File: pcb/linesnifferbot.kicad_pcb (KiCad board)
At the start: 2 copper layers, 100 x 99.5 mm, 78 parts, among them J10 CONN_01X09, J3 RxSel, J4 TxSel, J5 IntSelA, J6 IntSelB, J7 CONN_01X06, J8 Btn2EN, J9 LED2EN, Q1 Q_NMOS_GSD, SW1 SPDT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

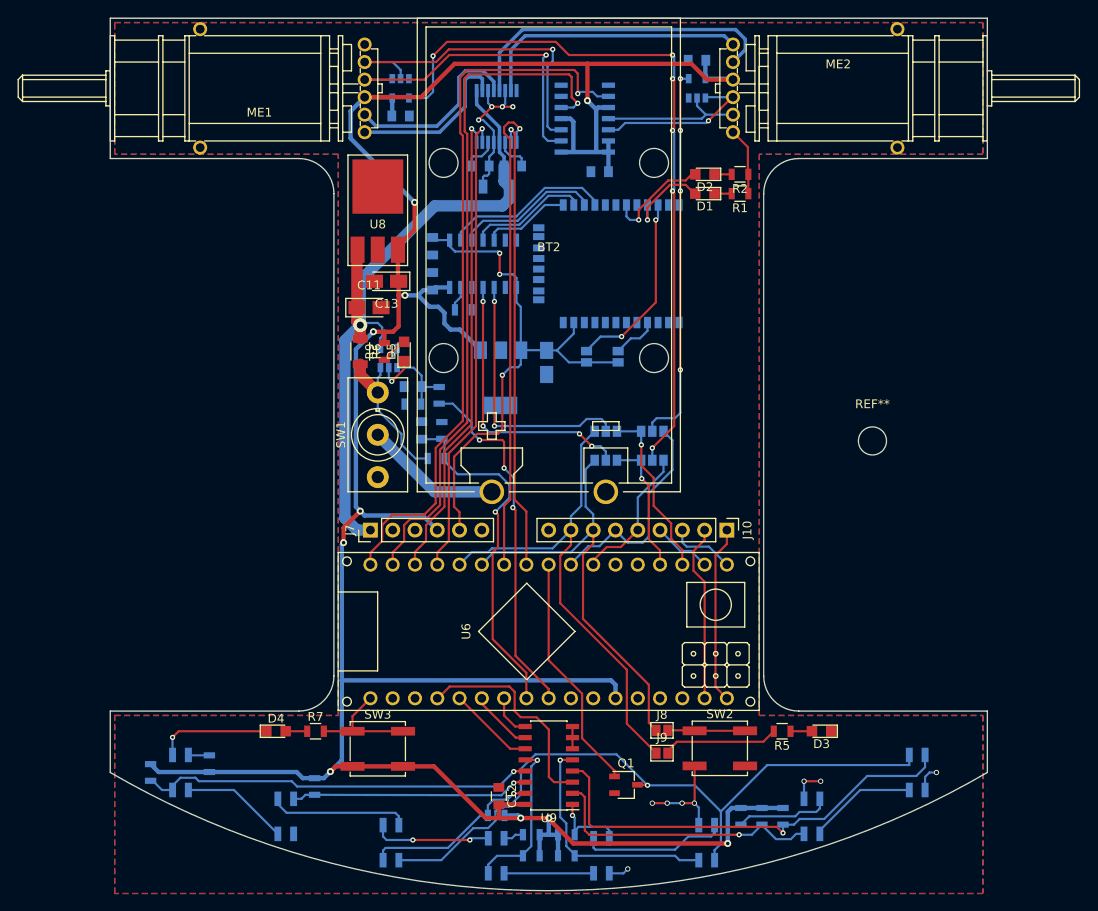
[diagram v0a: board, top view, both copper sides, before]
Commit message: Moved optical sensors closer together, and some other minor edits to the board
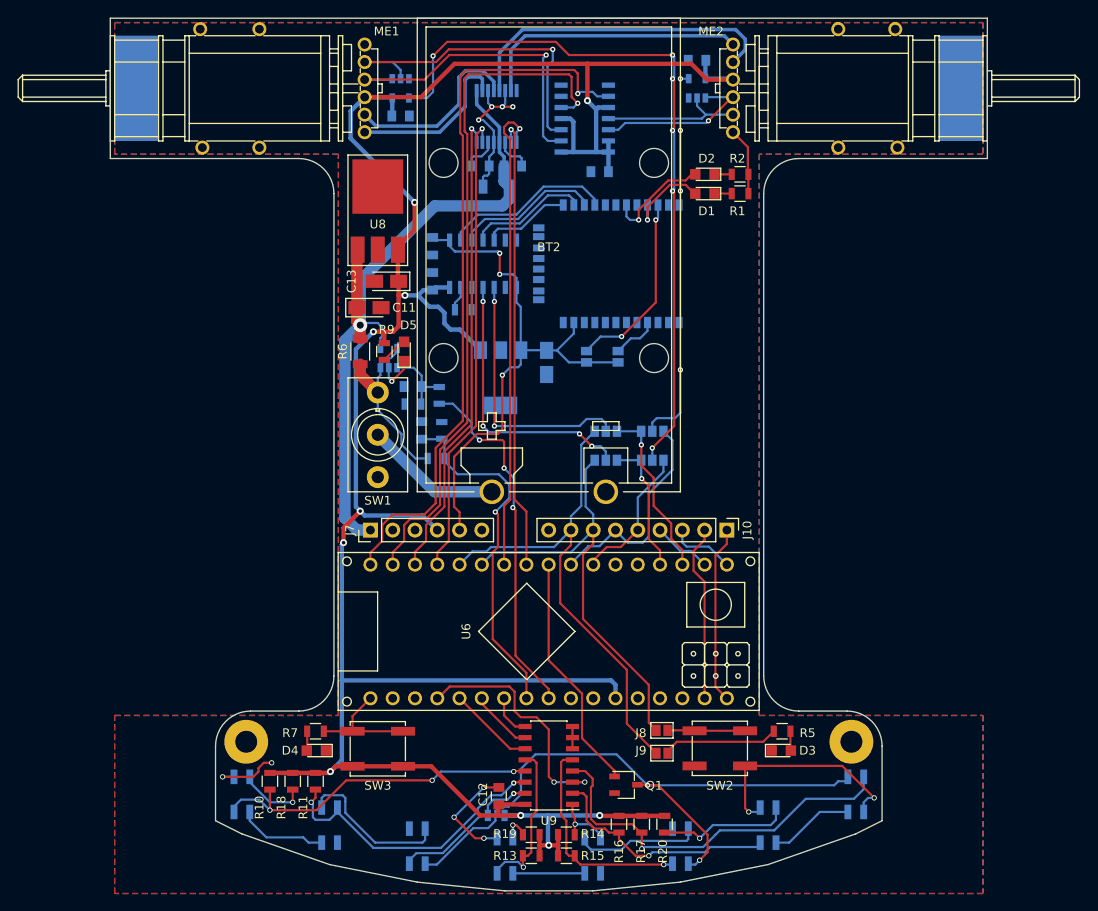
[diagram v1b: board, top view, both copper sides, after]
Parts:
- removed REF**: MountingHole_3.2mm_M3, Mounting_Holes:MountingHole_3.2mm_M3
- added ?: MountingHole_2.5mm_Pad, Mounting_Holes:MountingHole_2.5mm_Pad, F.Cu at (75.5, 142.5)
- added ?: MountingHole_2.5mm_Pad, Mounting_Holes:MountingHole_2.5mm_Pad, F.Cu at (144.5, 142.5)
- ME2: footprint PololuMotoEncoder -> Footprints:PololuMotoEncoder
- R10, R11, R13, R14, R15, R16, R17, R18, R19, R20: moved to F.Cu
- moved R16 16.3 mm to (118.0, 151.9)
- moved R17 16.1 mm to (120.6, 151.9)
- moved R10 13.6 mm to (78.2, 147.0)
- moved R18 9.71 mm to (80.8, 147.0), turned to 270 degrees
- moved R20 8.75 mm to (123.2, 151.9)
- moved S1 7.43 mm to (75.0, 148.5)
- moved S8 7.43 mm to (145.0, 148.5)
- moved S2 5.10 mm to (85.0, 152.0)
- moved S7 5.10 mm to (135.0, 152.0)
- moved D3 5.10 mm to (136.5, 143.5), turned to 0 degrees
- moved D4 5.10 mm to (83.5, 143.5), turned to 180 degrees
- moved S3 3.03 mm to (95.0, 154.4)
- moved S6 3.03 mm to (125.0, 154.4)
- moved S4 1.00 mm to (105.0, 155.5)
- moved S5 1.00 mm to (115.0, 155.5)
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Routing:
- net +5V: track 323.8 -> 291.9 mm
- net Net-(R17-Pad2): track 51.7 -> 45.2 mm
- net Net-(R11-Pad2): track 27.2 -> 33.6 mm, vias 1 -> 2
- net Net-(R18-Pad2): track 2.42 -> 8.10 mm, vias 0 -> 1
- net Net-(Q1-Pad3): track 78.6 -> 73.0 mm, vias 1 -> 2
- net Net-(R16-Pad2): track 32.2 -> 26.8 mm
- net Net-(R10-Pad2): track 45.2 -> 39.9 mm, vias 1 -> 3
- net Net-(R20-Pad2): track 10.9 -> 14.7 mm, vias 0 -> 1
- net Net-(R12-Pad2): track 21.0 -> 17.5 mm
- net Net-(U6-Pad21): track 24.9 -> 27.8 mm, vias 0 -> 2
- net Net-(S2-Pad2): track 16.0 -> 18.7 mm
- net Net-(S7-Pad2): track 12.5 -> 9.95 mm
- net Net-(R15-Pad2): track 27.4 -> 24.9 mm
- net Net-(S5-Pad2): track 16.7 -> 14.3 mm
- net Net-(S4-Pad2): track 10.2 -> 8.20 mm
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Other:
- outline, holes or cut-outs redrawn

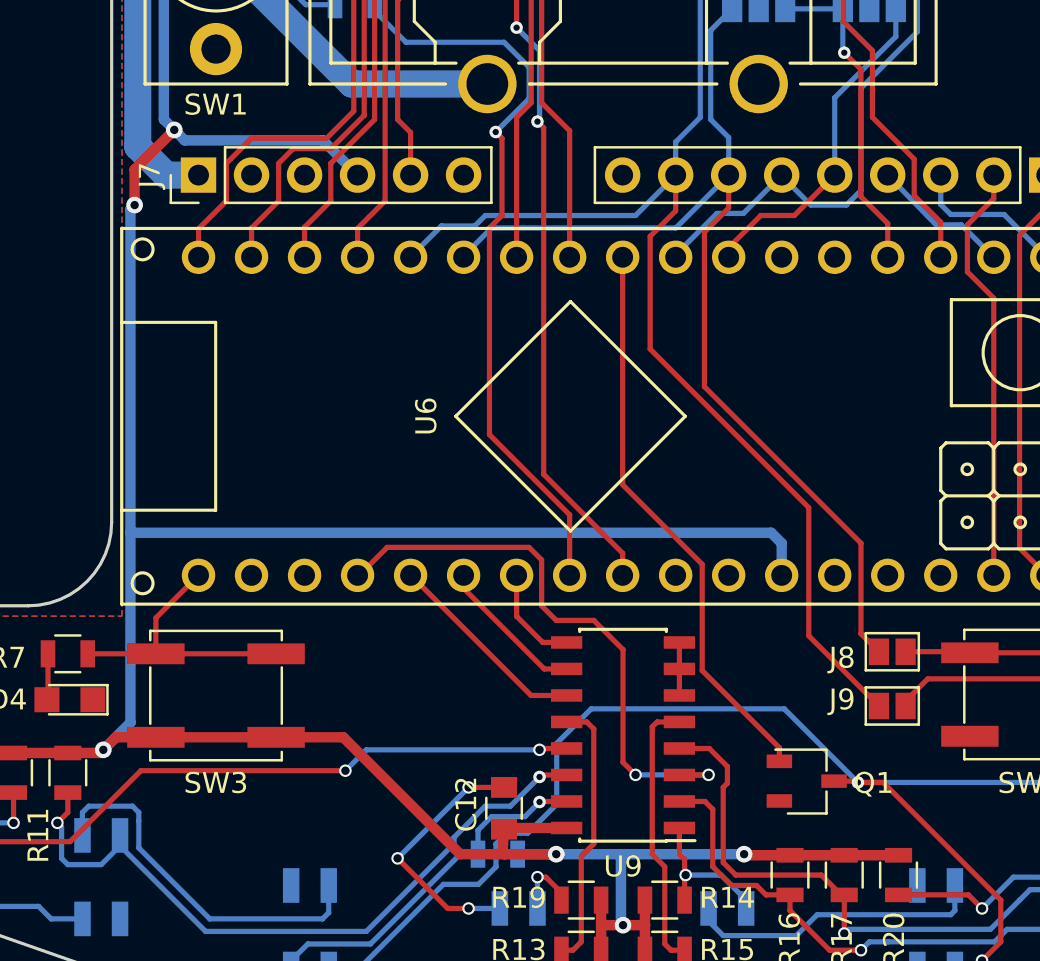
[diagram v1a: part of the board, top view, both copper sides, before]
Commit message: Added the BallCaster footprint to the PCB
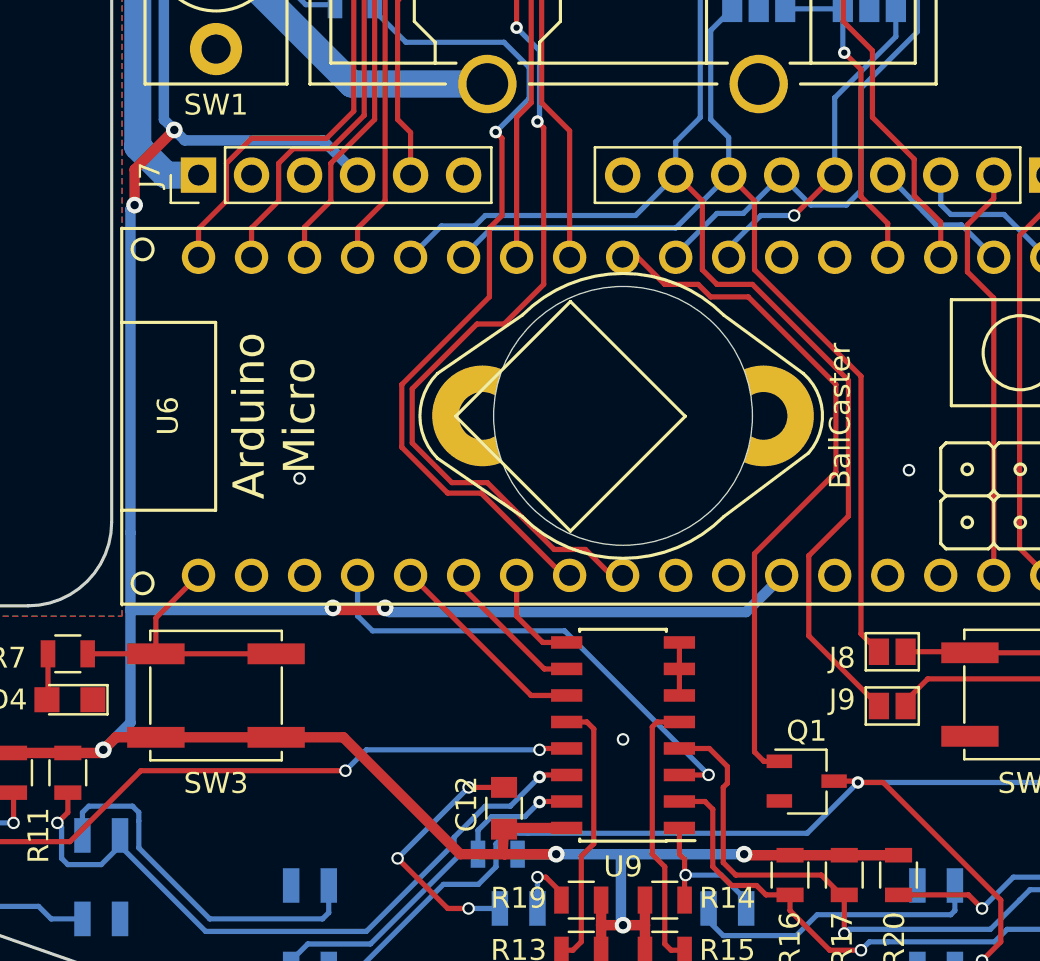
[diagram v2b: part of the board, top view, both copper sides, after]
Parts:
- added BallCaster: PololuBallCaster_3-8in, Footprints:PololuBallCaster_3-8in, F.Cu at (110.0, 129.9)
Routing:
- net Net-(R21-Pad2): track 41.3 -> 49.4 mm
- net Net-(Q1-Pad1): track 27.3 -> 33.3 mm
- net Net-(Q1-Pad3): track 73.0 -> 68.4 mm
- net Net-(C9-Pad1): track 40.5 -> 45.1 mm
- net Net-(U6-Pad21): track 27.8 -> 23.4 mm, vias 2 -> 1
- net IO8/A8: track 57.2 -> 58.8 mm
- net IO7(INT): track 49.9 -> 48.9 mm
- net +5V: track 291.9 -> 291.2 mm, vias 10 -> 12
- net I2C_SDA: track 16.8 -> 16.2 mm, vias 0 -> 1
- net GND: vias 12 -> 15
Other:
- board text added: "Arduino Micro"
- board text added: "Linesnifferbot v1 Nitromethane 2017"
